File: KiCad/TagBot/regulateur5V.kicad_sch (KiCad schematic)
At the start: 17 parts, among them U401 MP1475S

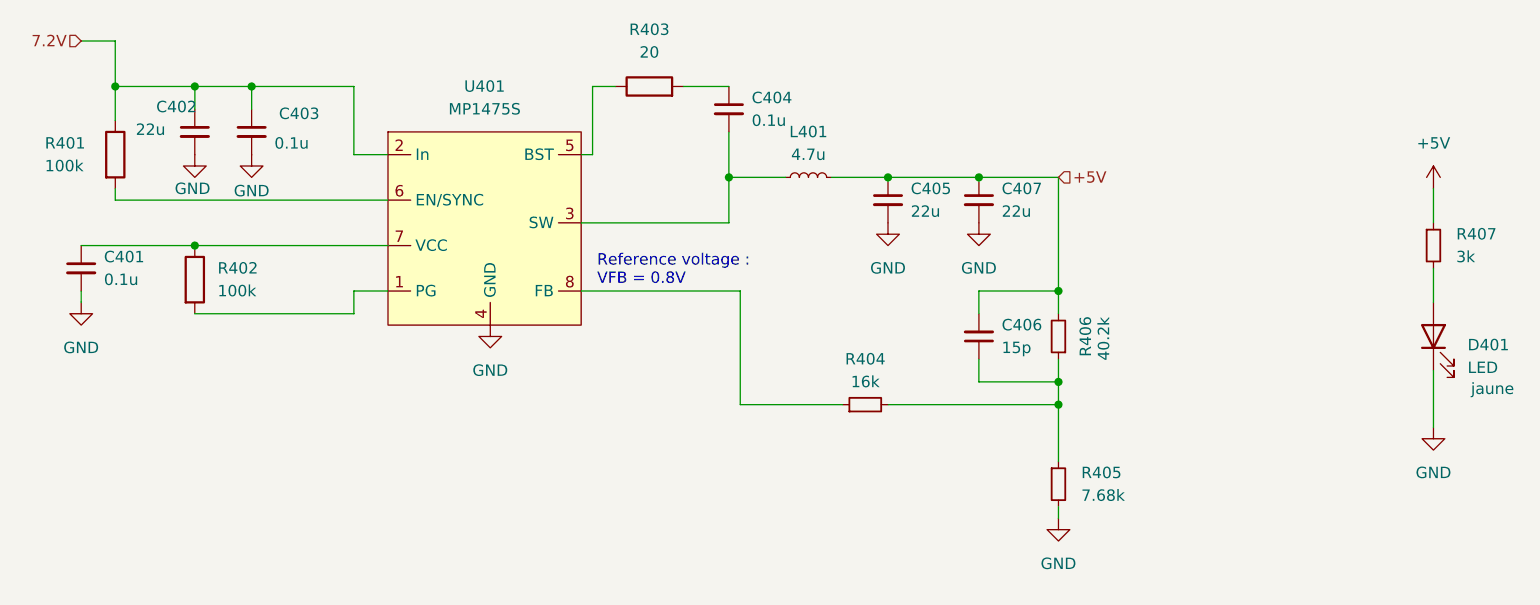
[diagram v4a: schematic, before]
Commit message: fixed switch footprint and genrated gerber files
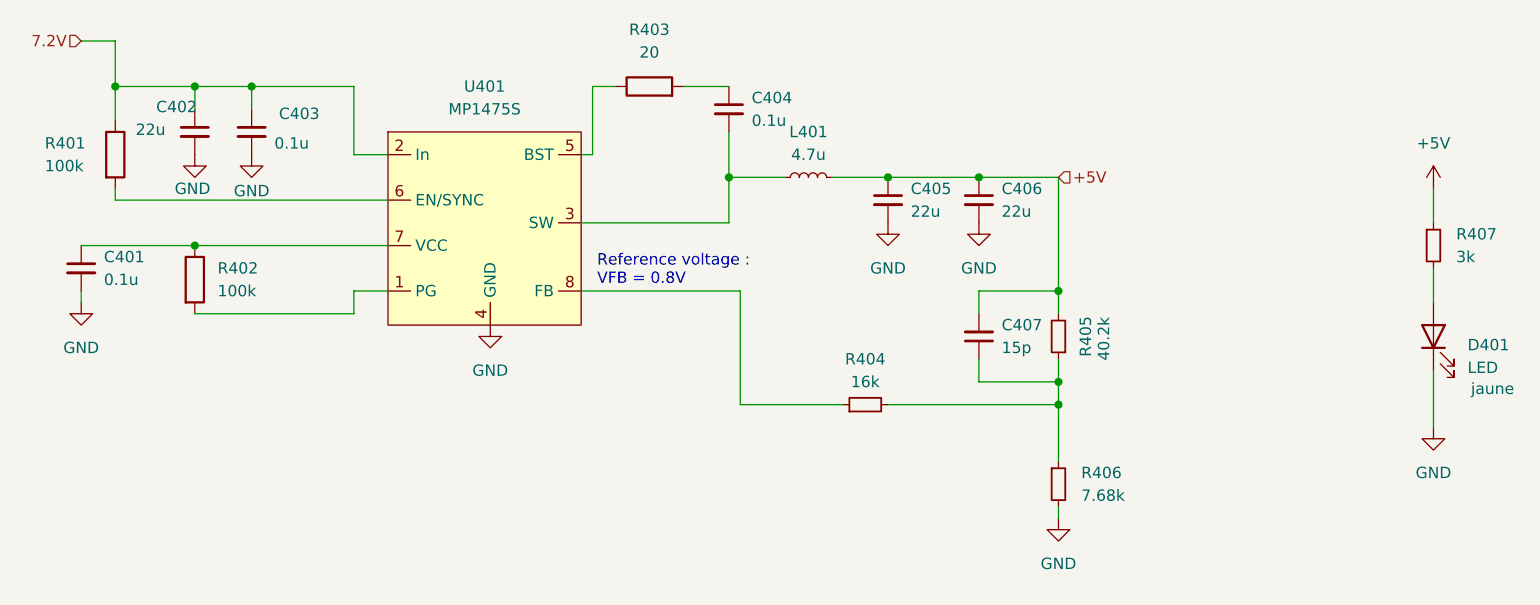
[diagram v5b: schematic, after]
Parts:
- renumbered C407 to C406, C406 to C407, R406 to R405, R405 to R406
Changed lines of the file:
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@@
 		(dnp no)
 		(fields_autoplaced yes)
-		(property "Reference" "C406"
+		(property "Reference" "C407"
 			(at 229.87 138.4235 0)
 			(effects
@@
 			(project "TagBot"
 				(path "/6db08f37-7cb3-4000-93f1-ba0d0ffbeb19/285c948d-5578-4bb8-8119-b871ade4552f"
-					(reference "C406")
+					(reference "C407")
 					(unit 1)
 				)
@@
 		(dnp no)
 		(fields_autoplaced yes)
-		(property "Reference" "C407"
+		(property "Reference" "C406"
 			(at 229.87 123.1962 0)
 			(effects
@@
 			(project "TagBot"
 				(path "/6db08f37-7cb3-4000-93f1-ba0d0ffbeb19/285c948d-5578-4bb8-8119-b871ade4552f"
-					(reference "C407")
+					(reference "C406")
 					(unit 1)
 				)
@@
 		(dnp no)
 		(fields_autoplaced yes)
-		(property "Reference" "#PWR0402"
+		(property "Reference" "#PWR0409"
 			(at 278.13 156.21 0)
 			(effects
@@
 			(project "TagBot"
 				(path "/6db08f37-7cb3-4000-93f1-ba0d0ffbeb19/285c948d-5578-4bb8-8119-b871ade4552f"
-					(reference "#PWR0402")
+					(reference "#PWR0409")
 					(unit 1)
 				)
@@
 		(on_board yes)
 		(dnp no)
-		(property "Reference" "#PWR0404"
+		(property "Reference" "#PWR0403"
 			(at 146.05 125.73 0)
 			(effects
@@
 			(project "TagBot"
 				(path "/6db08f37-7cb3-4000-93f1-ba0d0ffbeb19/285c948d-5578-4bb8-8119-b871ade4552f"
-					(reference "#PWR0404")
+					(reference "#PWR0403")
 					(unit 1)
 				)
@@
 		(dnp no)
 		(fields_autoplaced yes)
-		(property "Reference" "#PWR0405"
+		(property "Reference" "#PWR0401"
 			(at 127 142.24 0)
 			(effects
@@
 			(project "TagBot"
 				(path "/6db08f37-7cb3-4000-93f1-ba0d0ffbeb19/285c948d-5578-4bb8-8119-b871ade4552f"
-					(reference "#PWR0405")
+					(reference "#PWR0401")
 					(unit 1)
 				)
@@
 		(dnp no)
 		(fields_autoplaced yes)
-		(property "Reference" "#PWR0409"
+		(property "Reference" "#PWR0406"
 			(at 227.33 133.35 0)
 			(effects
@@
 			(project "TagBot"
 				(path "/6db08f37-7cb3-4000-93f1-ba0d0ffbeb19/285c948d-5578-4bb8-8119-b871ade4552f"
-					(reference "#PWR0409")
+					(reference "#PWR0406")
 					(unit 1)
 				)
@@
 		(dnp no)
 		(fields_autoplaced yes)
-		(property "Reference" "#PWR0401"
+		(property "Reference" "#PWR0408"
 			(at 278.13 127 0)
 			(effects
@@
 			(project "TagBot"
 				(path "/6db08f37-7cb3-4000-93f1-ba0d0ffbeb19/285c948d-5578-4bb8-8119-b871ade4552f"
-					(reference "#PWR0401")
+					(reference "#PWR0408")
 					(unit 1)
 				)
@@
 		(dnp no)
 		(fields_autoplaced yes)
-		(property "Reference" "R405"
+		(property "Reference" "R406"
 			(at 238.76 154.9399 0)
 			(effects
@@
 			(project "TagBot"
 				(path "/6db08f37-7cb3-4000-93f1-ba0d0ffbeb19/285c948d-5578-4bb8-8119-b871ade4552f"
-					(reference "R405")
+					(reference "R406")
 					(unit 1)
 				)
@@
 		(dnp no)
 		(fields_autoplaced yes)
-		(property "Reference" "#PWR0408"
+		(property "Reference" "#PWR0405"
 			(at 217.17 133.35 0)
 			(effects
@@
 			(project "TagBot"
 				(path "/6db08f37-7cb3-4000-93f1-ba0d0ffbeb19/285c948d-5578-4bb8-8119-b871ade4552f"
-					(reference "#PWR0408")
+					(reference "#PWR0405")
 					(unit 1)
 				)
@@
 		(dnp no)
 		(fields_autoplaced yes)
-		(property "Reference" "#PWR0406"
+		(property "Reference" "#PWR0404"
 			(at 172.72 144.78 0)
 			(effects
@@
 			(project "TagBot"
 				(path "/6db08f37-7cb3-4000-93f1-ba0d0ffbeb19/285c948d-5578-4bb8-8119-b871ade4552f"
-					(reference "#PWR0406")
+					(reference "#PWR0404")
 					(unit 1)
 				)
@@
 		(on_board yes)
 		(dnp no)
-		(property "Reference" "R406"
+		(property "Reference" "R405"
 			(at 239.268 139.7 90)
 			(effects
@@
 			(project "TagBot"
 				(path "/6db08f37-7cb3-4000-93f1-ba0d0ffbeb19/285c948d-5578-4bb8-8119-b871ade4552f"
-					(reference "R406")
+					(reference "R405")
 					(unit 1)
 				)
@@
 		(on_board yes)
 		(dnp no)
-		(property "Reference" "#PWR0403"
+		(property "Reference" "#PWR0402"
 			(at 139.7 125.73 0)
 			(effects
@@
 			(project "TagBot"
 				(path "/6db08f37-7cb3-4000-93f1-ba0d0ffbeb19/285c948d-5578-4bb8-8119-b871ade4552f"
-					(reference "#PWR0403")
-					(unit 1)
-				)
+					(reference "#PWR0402")
+					(unit 1)
+				)
